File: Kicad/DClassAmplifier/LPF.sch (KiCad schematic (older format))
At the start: 16 parts, among them J5 Conn_01x02, J6 Conn_01x02, U3 AD8567ARUZ

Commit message: PCB for input and added filter caps
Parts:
- added CF1: 100n, Capacitor_SMD:C_0805_2012Metric_Pad1.18x1.45mm_HandSolder, symbol Device:C_Small
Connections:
- net GND: now also CF1.2
- net VCC: now also CF1.1
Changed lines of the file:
@@
 Text HLabel 4400 6000 0    50   Input ~ 0
 SIG_IN
+$Comp
+L Device:C_Small CF1
+U 1 1 611D4F98
+P 5400 5225
+AR Path="/610C616D/611D4F98" Ref="CF1"  Part="1"
+AR Path="/611D4178/611D4F98" Ref="C?"  Part="1"
+F 0 "CF1" V 5171 5225 50  0000 C CNN
+F 1 "100n" V 5262 5225 50  0000 C CNN
+F 2 "Capacitor_SMD:C_0805_2012Metric_Pad1.18x1.45mm_HandSolder" H 5400 5225 50  0001 C CNN
+F 3 "~" H 5400 5225 50  0001 C CNN
+	1    5400 5225
+	1    0    0    -1
+$EndComp
+Connection ~ 5400 5125
+$Comp
+L power:GND #PWR?
+U 1 1 611D77EB
+P 5400 5325
+F 0 "#PWR?" H 5400 5075 50  0001 C CNN
+F 1 "GND" H 5405 5152 50  0000 C CNN
+F 2 "" H 5400 5325 50  0001 C CNN
+F 3 "" H 5400 5325 50  0001 C CNN
+	1    5400 5325
+	1    0    0    -1
+$EndComp
 $EndSCHEMATC

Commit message: Combined Board
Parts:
- removed J5, J6: Conn_01x02, TerminalBlock:TerminalBlock_bornier-2_P5.08mm, symbol Connector_Generic:Conn_01x02
- added JP1, JP2, JP3, JP4: SolderJumper_2_Open, Jumper:SolderJumper-2_P1.3mm_Open_RoundedPad1.0x1.5mm, symbol Jumper:SolderJumper_2_Open
- added R1, R14, R15, R4: 1Meg, Resistor_SMD:R_0603_1608Metric_Pad0.98x0.95mm_HandSolder, symbol Device:R_Small
- added R12, R13, R2, R3: 1k, Resistor_SMD:R_0603_1608Metric_Pad0.98x0.95mm_HandSolder, symbol Device:R_Small
- C3: renamed from CF1; footprint Capacitor_SMD:C_0805_2012Metric_Pad1.18x1.45mm_HandSolder -> Capacitor_SMD:C_0603_1608Metric_Pad1.08x0.95mm_HandSolder
- C5: renamed from C10; footprint Capacitor_SMD:C_0805_2012Metric_Pad1.18x1.45mm_HandSolder -> Capacitor_SMD:C_0603_1608Metric_Pad1.08x0.95mm_HandSolder
- TP10: footprint TestPoint:TestPoint_Pad_D2.0mm -> TestPoint:TestPoint_THTPad_D1.5mm_Drill0.7mm
- renumbered C13 to C4, C14 to C6, C11 to C7, C12 to C8, R17 to R10, R14 to R11, R15 to R5, R13 to R6, R18 to R7, R19 to R8, R16 to R9, U3 to U1
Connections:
- net BIASED_SIG: now also U1.1 (OUTA), JP2.1 (A), R1.1, R2.2; no longer U1.6 (-INB), U1.7 (OUTB)
- net Filter_FirstStage: now also JP1.1 (A), R3.2; no longer C4.1, U1.13 (-IND)
- net GND: now also R1.2, R14.2, R15.2, R4.1
- net SIG_OUT: now also JP4.1 (A), R13.2, R15.1; no longer C7.2, U1.9 (-INC)
- net VREF: now also U1.7 (OUTB), JP3.1 (A), R12.2, R14.1; no longer U1.1 (OUTA), U1.2 (-INA)
- net at R11.1, R6.2: now also U1.5 (+INB); no longer U1.3 (+INA)
- net at C5.1, R5.2: now also U1.3 (+INA); no longer U1.5 (+INB)
- new net: C4.1, JP1.2 (B), R3.1, R4.2, U1.13 (-IND)
- new net: JP2.2 (B), R2.1, U1.2 (-INA)
- new net: JP3.2 (B), R12.1, U1.6 (-INB)
- new net: C7.2, JP4.2 (B), R13.1, U1.9 (-INC)
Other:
- moved on the sheet: C3, C5, C7, R11, R5, R6, TP10

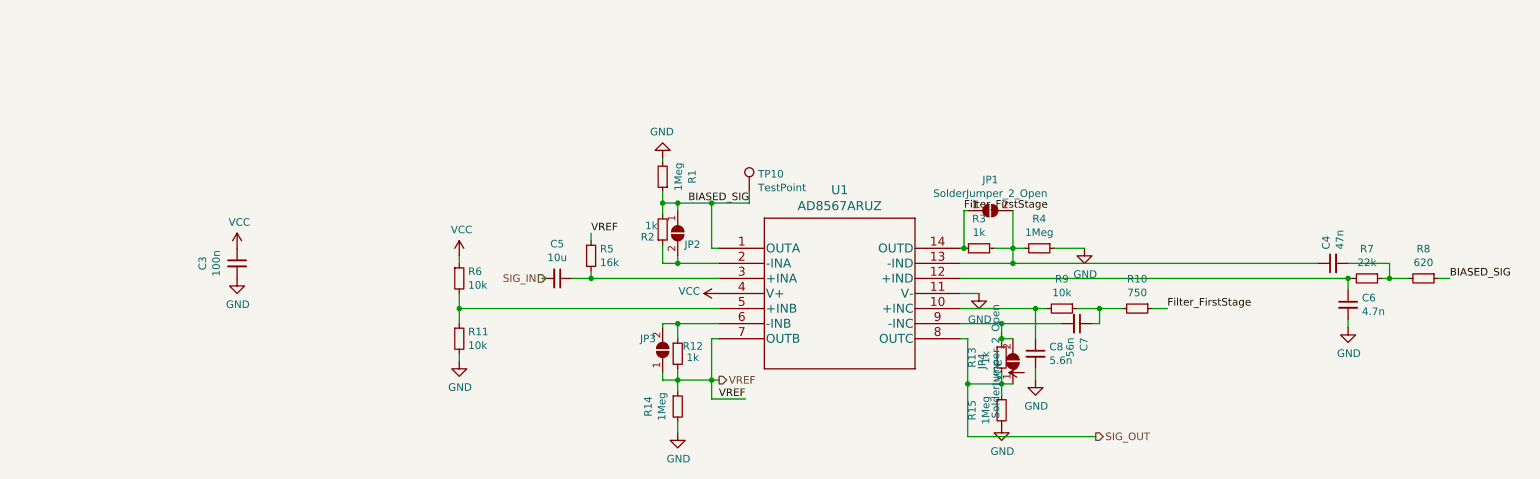
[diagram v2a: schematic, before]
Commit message: Add 10V Reg and Reroute
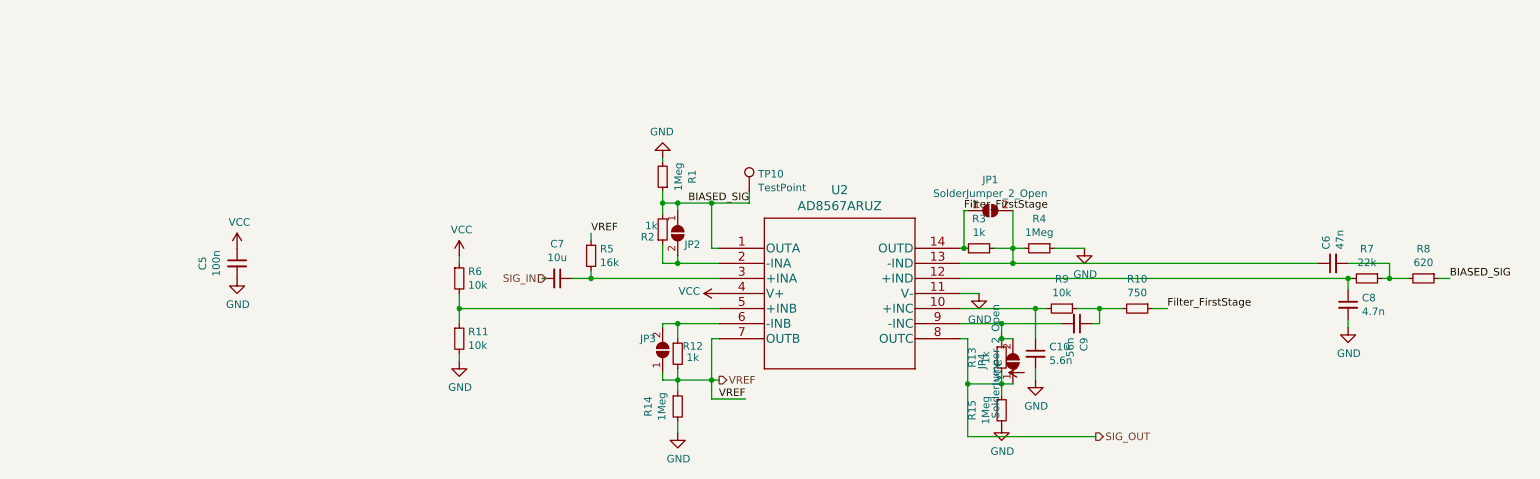
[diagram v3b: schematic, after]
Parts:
- renumbered C8 to C10, C3 to C5, C4 to C6, C5 to C7, C6 to C8, C7 to C9, U1 to U2
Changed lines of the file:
@@
 $EndComp
 $Comp
-L Device:C_Small C6
+L Device:C_Small C8
 U 1 1 611A751B
 P 9800 5200
-F 0 "C6" H 9892 5246 50  0000 L CNN
+F 0 "C8" H 9892 5246 50  0000 L CNN
 F 1 "4.7n" H 9892 5155 50  0000 L CNN
 F 2 "Capacitor_SMD:C_0603_1608Metric_Pad1.08x0.95mm_HandSolder" H 9800 5200 50  0001 C CNN
@@
 	9800 5300 9800 5350
 $Comp
-L power:GND #PWR017
+L power:GND #PWR020
 U 1 1 611AAC29
 P 9800 5350
-F 0 "#PWR017" H 9800 5100 50  0001 C CNN
+F 0 "#PWR020" H 9800 5100 50  0001 C CNN
 F 1 "GND" H 9805 5177 50  0000 C CNN
 F 2 "" H 9800 5350 50  0001 C CNN
@@
 $EndComp
 $Comp
-L Device:C_Small C8
+L Device:C_Small C10
 U 1 1 611BBE57
 P 7725 5525
-F 0 "C8" H 7817 5571 50  0000 L CNN
+F 0 "C10" H 7817 5571 50  0000 L CNN
 F 1 "5.6n" H 7817 5480 50  0000 L CNN
 F 2 "Capacitor_SMD:C_0603_1608Metric_Pad1.08x0.95mm_HandSolder" H 7725 5525 50  0001 C CNN
@@
 	8600 5225 8500 5225
 $Comp
-L Device:C_Small C7
+L Device:C_Small C9
 U 1 1 611C0153
 P 8000 5325
-F 0 "C7" H 8092 5371 50  0000 L CNN
+F 0 "C9" H 8092 5371 50  0000 L CNN
 F 1 "56n" H 8092 5280 50  0000 L CNN
 F 2 "Capacitor_SMD:C_0603_1608Metric_Pad1.08x0.95mm_HandSolder" H 8000 5325 50  0001 C CNN
@@
 $EndComp
 $Comp
-L power:GND #PWR020
+L power:GND #PWR023
 U 1 1 611C31DE
 P 7725 5700
-F 0 "#PWR020" H 7725 5450 50  0001 C CNN
+F 0 "#PWR023" H 7725 5450 50  0001 C CNN
 F 1 "GND" H 7730 5527 50  0000 C CNN
 F 2 "" H 7725 5700 50  0001 C CNN
@@
 P 5625 4825
 AR Path="/61100E74" Ref="U?"  Part="1"
-AR Path="/610C616D/61100E74" Ref="U1"  Part="1"
-F 0 "U1" H 6425 5212 60  0000 C CNN
+AR Path="/610C616D/61100E74" Ref="U2"  Part="1"
+F 0 "U2" H 6425 5212 60  0000 C CNN
 F 1 "AD8567ARUZ" H 6425 5106 60  0000 C CNN
 F 2 "AD8567ARUZ:AD8567ARUZ" H 6425 5065 60  0001 C CNN
@@
 $EndComp
 $Comp
-L power:GND #PWR016
+L power:GND #PWR019
 U 1 1 61106B09
 P 7350 5125
-AR Path="/610C616D/61106B09" Ref="#PWR016"  Part="1"
+AR Path="/610C616D/61106B09" Ref="#PWR019"  Part="1"
 AR Path="/611D4178/61106B09" Ref="#PWR?"  Part="1"
-F 0 "#PWR016" H 7350 4875 50  0001 C CNN
+F 0 "#PWR019" H 7350 4875 50  0001 C CNN
 F 1 "GND" H 7355 4952 50  0000 C CNN
 F 2 "" H 7350 5125 50  0001 C CNN
@@
 	7250 4825 7225 4825
 $Comp
-L Device:C_Small C4
+L Device:C_Small C6
 U 1 1 611A7CBC
 P 9700 4925
-F 0 "C4" H 9792 4971 50  0000 L CNN
+F 0 "C6" H 9792 4971 50  0000 L CNN
 F 1 "47n" H 9792 4880 50  0000 L CNN
 F 2 "Capacitor_SMD:C_0603_1608Metric_Pad1.08x0.95mm_HandSolder" H 9700 4925 50  0001 C CNN
@@
 $EndComp
 $Comp
-L Device:C_Small C3
+L Device:C_Small C5
 U 1 1 611D4F98
 P 2425 4925
-AR Path="/610C616D/611D4F98" Ref="C3"  Part="1"
+AR Path="/610C616D/611D4F98" Ref="C5"  Part="1"
 AR Path="/611D4178/611D4F98" Ref="C?"  Part="1"
-F 0 "C3" V 2196 4925 50  0000 C CNN
+F 0 "C5" V 2196 4925 50  0000 C CNN
 F 1 "100n" V 2287 4925 50  0000 C CNN
 F 2 "Capacitor_SMD:C_0603_1608Metric_Pad1.08x0.95mm_HandSolder" H 2425 4925 50  0001 C CNN
@@
 $EndComp
 $Comp
-L power:GND #PWR014
+L power:GND #PWR017
 U 1 1 611D77EB
 P 2425 5025
-F 0 "#PWR014" H 2425 4775 50  0001 C CNN
+F 0 "#PWR017" H 2425 4775 50  0001 C CNN
 F 1 "GND" H 2430 4852 50  0000 C CNN
 F 2 "" H 2425 5025 50  0001 C CNN
@@
 $EndComp
 $Comp
-L power:GND #PWR012
+L power:GND #PWR015
 U 1 1 6117BB16
 P 8050 4825
-F 0 "#PWR012" H 8050 4575 50  0001 C CNN
+F 0 "#PWR015" H 8050 4575 50  0001 C CNN
 F 1 "GND" H 8055 4652 50  0000 C CNN
 F 2 "" H 8050 4825 50  0001 C CNN
@@
 	8050 4825 7850 4825
 $Comp
-L power:VCC #PWR011
+L power:VCC #PWR014
 U 1 1 61106B01
 P 2425 4825
-AR Path="/610C616D/61106B01" Ref="#PWR011"  Part="1"
+AR Path="/610C616D/61106B01" Ref="#PWR014"  Part="1"
 AR Path="/611D4178/61106B01" Ref="#PWR?"  Part="1"
-F 0 "#PWR011" H 2425 4675 50  0001 C CNN
+F 0 "#PWR014" H 2425 4675 50  0001 C CNN
 F 1 "VCC" H 2440 4998 50  0000 C CNN
 F 2 "" H 2425 4825 50  0001 C CNN
@@
 $EndComp
 $Comp
-L power:GND #PWR010
+L power:GND #PWR013
 U 1 1 612E7D6A
 P 5250 4225
-F 0 "#PWR010" H 5250 3975 50  0001 C CNN
+F 0 "#PWR013" H 5250 3975 50  0001 C CNN
 F 1 "GND" H 5255 4052 50  0000 C CNN
 F 2 "" H 5250 4225 50  0001 C CNN
@@
 $EndComp
 $Comp
-L power:VCC #PWR019
+L power:VCC #PWR022
 U 1 1 6132C09D
 P 7650 5650
-AR Path="/610C616D/6132C09D" Ref="#PWR019"  Part="1"
+AR Path="/610C616D/6132C09D" Ref="#PWR022"  Part="1"
 AR Path="/611D4178/6132C09D" Ref="#PWR?"  Part="1"
-F 0 "#PWR019" H 7650 5500 50  0001 C CNN
+F 0 "#PWR022" H 7650 5500 50  0001 C CNN
 F 1 "VCC" H 7665 5823 50  0000 C CNN
 F 2 "" H 7650 5650 50  0001 C CNN
@@
 $EndComp
 $Comp
-L power:GND #PWR021
+L power:GND #PWR024
 U 1 1 6132C085
 P 7500 6000
-F 0 "#PWR021" H 7500 5750 50  0001 C CNN
+F 0 "#PWR024" H 7500 5750 50  0001 C CNN
 F 1 "GND" H 7505 5827 50  0000 C CNN
 F 2 "" H 7500 6000 50  0001 C CNN
@@
 P 3900 4875
 AR Path="/611D4178/61106B43" Ref="#PWR?"  Part="1"
-AR Path="/610C616D/61106B43" Ref="#PWR013"  Part="1"
-F 0 "#PWR013" H 3900 4725 50  0001 C CNN
+AR Path="/610C616D/61106B43" Ref="#PWR016"  Part="1"
+F 0 "#PWR016" H 3900 4725 50  0001 C CNN
 F 1 "VCC" H 3915 5048 50  0000 C CNN
 F 2 "" H 3900 4875 50  0001 C CNN
@@
 P 3900 5575
 AR Path="/611D4178/61106B3C" Ref="#PWR?"  Part="1"
-AR Path="/610C616D/61106B3C" Ref="#PWR018"  Part="1"
-F 0 "#PWR018" H 3900 5325 50  0001 C CNN
+AR Path="/610C616D/61106B3C" Ref="#PWR021"  Part="1"
+F 0 "#PWR021" H 3900 5325 50  0001 C CNN
 F 1 "GND" H 3905 5402 50  0000 C CNN
 F 2 "" H 3900 5575 50  0001 C CNN
@@
 Connection ~ 5350 5700
 $Comp
-L power:GND #PWR022
+L power:GND #PWR025
 U 1 1 6116176E
 P 5350 6050
-F 0 "#PWR022" H 5350 5800 50  0001 C CNN
+F 0 "#PWR025" H 5350 5800 50  0001 C CNN
 F 1 "GND" H 5355 5877 50  0000 C CNN
 F 2 "" H 5350 6050 50  0001 C CNN
@@
 	4650 5025 4775 5025
 $Comp
-L Device:C_Small C5
+L Device:C_Small C7
 U 1 1 61106B1C
 P 4550 5025
-AR Path="/610C616D/61106B1C" Ref="C5"  Part="1"
+AR Path="/610C616D/61106B1C" Ref="C7"  Part="1"
 AR Path="/611D4178/61106B1C" Ref="C?"  Part="1"
-F 0 "C5" V 4321 5025 50  0000 C CNN
+F 0 "C7" V 4321 5025 50  0000 C CNN
 F 1 "10u" V 4412 5025 50  0000 C CNN
 F 2 "Capacitor_SMD:C_0603_1608Metric_Pad1.08x0.95mm_HandSolder" H 4550 5025 50  0001 C CNN
@@
 	4775 5025 5625 5025
 $Comp
-L power:VCC #PWR015
+L power:VCC #PWR018
 U 1 1 6154BCB6
 P 5625 5125
-F 0 "#PWR015" H 5625 4975 50  0001 C CNN
+F 0 "#PWR018" H 5625 4975 50  0001 C CNN
 F 1 "VCC" V 5640 5252 50  0000 L CNN
 F 2 "" H 5625 5125 50  0001 C CNN
